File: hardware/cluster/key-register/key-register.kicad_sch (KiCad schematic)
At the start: 2 parts

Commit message: First PCB: the left-hand key board, placed from the body CAD and routed
- tools/pcb.py: a board's first layout from its KiCad sheets (netlist,
  footprints) and the body CAD's new exports (key-board outline DXF,
  switch and ribbon-connector positions); then the .kicad_pcb is source.
  check = KiCad DRC with schematic parity + switches where the CAD puts
  them; render = 3D both sides, 2D copper, and fab/ (Gerbers, drill,
  placement), ledgered in hardware/SHEETS.csv. tools/kicad.py check runs it.
- tools/pcb_route.py: a small two-layer grid router for simple boards;
  ground routed as a net plus pours and stitching vias.
- key-board-lh: 24 parts, all nets routed; KiCad DRC 0 errors, schematic
  parity clean (one stock-footprint silkscreen warning). Tested: a switch
  moved 1 mm fails the check.
- Footprints on the sheets; hardware/lib/woody.pretty holds the KS-33
  footprint (marbastlib, banked) with Gateron's STEP lifted by
  switch.pcb_below_seat. J-CHAIN's stand-in is Molex 200528-0120.
- Findings, recorded in tooling.md §4 and DESIGN.md: the ribbon connector
  needs 6.7 mm, the CAD envelope is 5.5; KS-33 pins show only ~0.1 mm
  below a 1.6 mm board (1.2 mm would leave ~0.5).
- setup-env.sh installs footprints, rsvg, shapely and repairs an empty
  global fp-lib-table.

Co-Authored-By: Claude Opus 5.5 <noreply@anthropic.com>
Claude-Session: https://claude.ai/code/session_01LmB4muFXnoLprWX4JzuJ5A
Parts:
- C-DECOUPLE-165: footprint (none) -> Capacitor_SMD:C_0805_2012Metric
- U-KEYS: footprint (none) -> Package_SO:SOIC-16_3.9x9.9mm_P1.27mm
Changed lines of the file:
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@@
     (property "Reference" "U-KEYS" (at 93.98 91.44 0) (effects (font (size 1.27 1.27))))
     (property "Value" "74HC165" (at 93.98 132.08 0) (effects (font (size 1.27 1.27))))
-    (property "Footprint" "" (at 101.6 110.49 0) (effects (font (size 1.27 1.27)) hide))
+    (property "Footprint" "Package_SO:SOIC-16_3.9x9.9mm_P1.27mm" (at 101.6 110.49 0) (effects (font (size 1.27 1.27)) hide))
     (property "Datasheet" "" (at 101.6 110.49 0) (effects (font (size 1.27 1.27)) hide))
     (property "Row" "U-KEYS" (at 101.6 110.49 0) (effects (font (size 1.27 1.27)) hide))
@@
     (property "Reference" "C-DECOUPLE-165" (at 129.54 78.74 0) (effects (font (size 1.27 1.27)) (justify left)))
     (property "Value" "100nF" (at 129.54 81.28 0) (effects (font (size 1.27 1.27)) (justify left)))
-    (property "Footprint" "" (at 128.27 83.82 0) (effects (font (size 1.27 1.27)) hide))
+    (property "Footprint" "Capacitor_SMD:C_0805_2012Metric" (at 128.27 83.82 0) (effects (font (size 1.27 1.27)) hide))
     (property "Datasheet" "" (at 127.0 80.01 0) (effects (font (size 1.27 1.27)) hide))
     (property "Row" "C-DECOUPLE-165" (at 127.0 80.01 0) (effects (font (size 1.27 1.27)) hide))

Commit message: LH key board as the worked example: orderable, labelled, testable
- Samtec full prints banked (SHF header, FFSD cable); the header's true
  dimensions replace the catalogue estimates (body.yaml boards.chain_*), and
  the cable is ordered -RN2 (notch reversed on the key-board end): both
  sockets' cables leave downward, the ribbon runs flat, and key-board pin =
  13 - main-board pin. The same-day 12-n/14-n map was wrong and is undone in
  the sheets, the interface netlist and the docs (history in notes.md).
- Model: the hairpin's legs follow the cable's real exit - the main board's
  on the board, clear of the thumb switches' poles; 0 DRC FAILs, 0 clashes.
- Sheets: Manufacturer/MPN/LCSC/Assembly fields from JLC's parts API (JLC
  and LCSC pages banked in datasheets/fab and the manifest); five bring-up
  test pads per key board (TP-CHAIN, copper only).
- pcb.py: JLC's limits in the DRC (layout.yaml fab:), which grew the vias
  and J-CHAIN's pads to the 0.18 mm ring; HASL lead-free in the stackup and
  Gerber job; a generated parts-side silkscreen; the JLC BOM, CPL and
  hand-assembly list in fab/, ledgered against board and sheets.
- Router: a real rip-up (blockers removed too); plated holes no longer wall
  off their own pads.
- hardware/boards/key-board-lh/README.md: sources, ordering, hand assembly,
  bring-up, open items. tooling.md and lib README follow.
All checks pass: CAD, DRC (0/0), KiCad, staleness, BOM, netlist, datasheets.

Co-Authored-By: Claude Opus 5.5 <noreply@anthropic.com>
Claude-Session: https://claude.ai/code/session_01LmB4muFXnoLprWX4JzuJ5A
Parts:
- C-DECOUPLE-165: Assembly (none) -> machine; LCSC (none) -> C49678; MPN (none) -> CC0805KRX7R9BB104; Manufacturer (none) -> YAGEO
- U-KEYS: Assembly (none) -> machine; LCSC (none) -> C5613; MPN (none) -> 74HC165D,653; Manufacturer (none) -> Nexperia
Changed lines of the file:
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@@
     (property "Note" "74HC AND NOT 74LVC, and that is load-bearing: HC's slow edges keep each hop an ordinary lumped load. Bit order out is H first, then G F E D C B A" (at 101.6 110.49 0) (effects (font (size 1.27 1.27)) hide))
     (property "Pins_source" "SOIC-16 pin-out, datasheets/logic/74HC165-ti-scls116e.pdf p.1; library names checked" (at 101.6 110.49 0) (effects (font (size 1.27 1.27)) hide))
+    (property "Manufacturer" "Nexperia" (at 101.6 110.49 0) (effects (font (size 1.27 1.27)) hide))
+    (property "MPN" "74HC165D,653" (at 101.6 110.49 0) (effects (font (size 1.27 1.27)) hide))
+    (property "LCSC" "C5613" (at 101.6 110.49 0) (effects (font (size 1.27 1.27)) hide))
+    (property "Assembly" "machine" (at 101.6 110.49 0) (effects (font (size 1.27 1.27)) hide))
     (pin "1")
     (pin "10")
@@
     (property "Pins" "1=1 2=2" (at 127.0 80.01 0) (effects (font (size 1.27 1.27)) hide))
     (property "Note" "AT the package, on this board. A 74x165's output edges brown out a local rail with no reservoir, and on a key board the ribbon is the only other source" (at 127.0 80.01 0) (effects (font (size 1.27 1.27)) hide))
+    (property "Manufacturer" "YAGEO" (at 127.0 80.01 0) (effects (font (size 1.27 1.27)) hide))
+    (property "MPN" "CC0805KRX7R9BB104" (at 127.0 80.01 0) (effects (font (size 1.27 1.27)) hide))
+    (property "LCSC" "C49678" (at 127.0 80.01 0) (effects (font (size 1.27 1.27)) hide))
+    (property "Assembly" "machine" (at 127.0 80.01 0) (effects (font (size 1.27 1.27)) hide))
     (pin "1")
     (pin "2")

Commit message: WIP: layout-side fixes (networks as T, via-in-pad, segment merge, silk, stackup, TP-SER, drills)
Co-Authored-By: Claude Opus 5.5 <noreply@anthropic.com>
Claude-Session: https://claude.ai/code/session_01LmB4muFXnoLprWX4JzuJ5A
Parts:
- U-KEYS: Pins_source SOIC-16 pin-out, datasheets/logic/74HC165-ti-scls116e.pdf p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 -> SO16 (SOT109-1) pin-out, datasheets/logic/74HC165-nexperia.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
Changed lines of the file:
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@@
     (property "Pins" "SHLD=1(~{PL}) CLK=2(CP) CLKINH=15(~{CE}) QH_BAR=7(~{Q7}) GND=8(GND) SER=10(DS) QH=9(Q7) VCC=16(VCC) A=11(D0) B=12(D1) C=13(D2) D=14(D3) E=3(D4) F=4(D5) G=5(D6) H=6(D7)" (at 101.6 110.49 0) (effects (font (size 1.27 1.27)) hide))
     (property "Note" "74HC AND NOT 74LVC, and that is load-bearing: HC's slow edges keep each hop an ordinary lumped load. Bit order out is H first, then G F E D C B A" (at 101.6 110.49 0) (effects (font (size 1.27 1.27)) hide))
-    (property "Pins_source" "SOIC-16 pin-out, datasheets/logic/74HC165-ti-scls116e.pdf p.1; library names checked" (at 101.6 110.49 0) (effects (font (size 1.27 1.27)) hide))
+    (property "Pins_source" "SO16 (SOT109-1) pin-out, datasheets/logic/74HC165-nexperia.pdf p.3 figure and p.4 Table 2; library names checked" (at 101.6 110.49 0) (effects (font (size 1.27 1.27)) hide))
     (property "Manufacturer" "Nexperia" (at 101.6 110.49 0) (effects (font (size 1.27 1.27)) hide))
     (property "MPN" "74HC165D,653" (at 101.6 110.49 0) (effects (font (size 1.27 1.27)) hide))

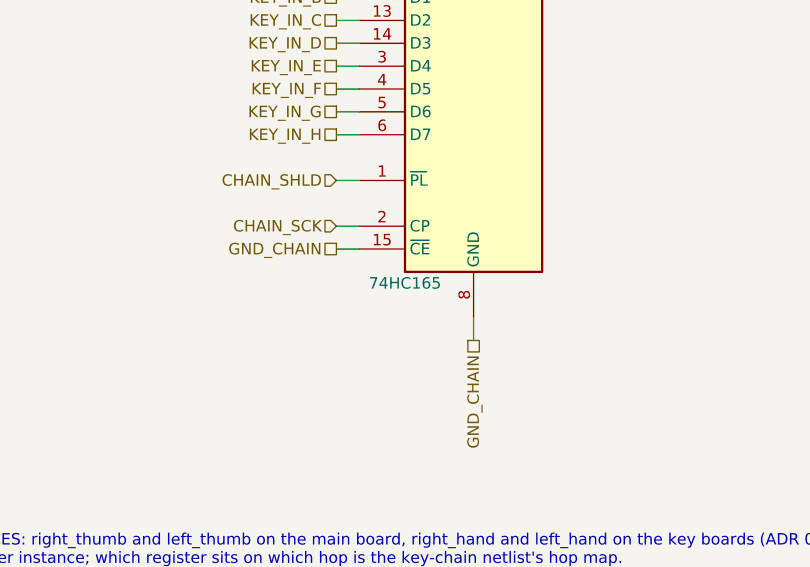
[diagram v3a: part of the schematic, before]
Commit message: Register becomes the SN74HCS165; key-board standoff gets its washer
The owner's two decisions after the LH wave:

SN74HCS165 (TI, Schmitt-trigger inputs, no input transition-rate limit):
- key-register.kicad_sch U-KEYS: value, Manufacturer, MPN SN74HCS165DR,
  LCSC C2864745, Pins_source (TI p.3), Note; same SOIC-16 and symbol.
- U-KEYS row: what the part must be, and that a substitute needs Schmitt
  inputs with no rate limit (not a 74HC165, not a 74LV165A).
- key-release-time 119.9 -> 138.7 us and key-press-time 5.92 -> 9.87 us,
  against TI's thresholds at their guaranteed extremes (no 3.3 V row: the
  table's largest VT+ and smallest VT- ratios). Old spellings grepped first
  and moved into forbidden; the four patterns that matched the new value
  removed. The release is now just over half a scan, which changes no
  conclusion; the 10k trade recomputed (647 us).
- key-switch-network.md derives both against the HCS165; the retired HC165
  derivation moved to notes.md. ADR 0001 amended and its table cites the
  figures.

The standoff and washer:
- MSO4-M2-3 chosen, with an ISO 7092 / DIN 433 M2 washer under the board.
  Head flush in the plate, so the key boards' depth is standoff length +
  washer: switch.pcb_below_seat 3.4 -> 3.3, checked by a new rule, with the
  worst-case tolerance stack printed as a NOTE.
- The thumb switches keep their own depth, switch.thumb_pcb_below_seat:
  sharing the parameter moved them into the LED strip (clash.txt caught it).
- MECH-KB-WASHER row; MECH-KB-STANDOFF names the part and its US sources;
  MECH-KB-SCREW M2 x 4. The PCB's copper keep-out covers the washer.
- LH board re-laid out, checked (0 errors) and rendered.

Co-Authored-By: Claude Opus 5.5 <noreply@anthropic.com>
Claude-Session: https://claude.ai/code/session_01LmB4muFXnoLprWX4JzuJ5A
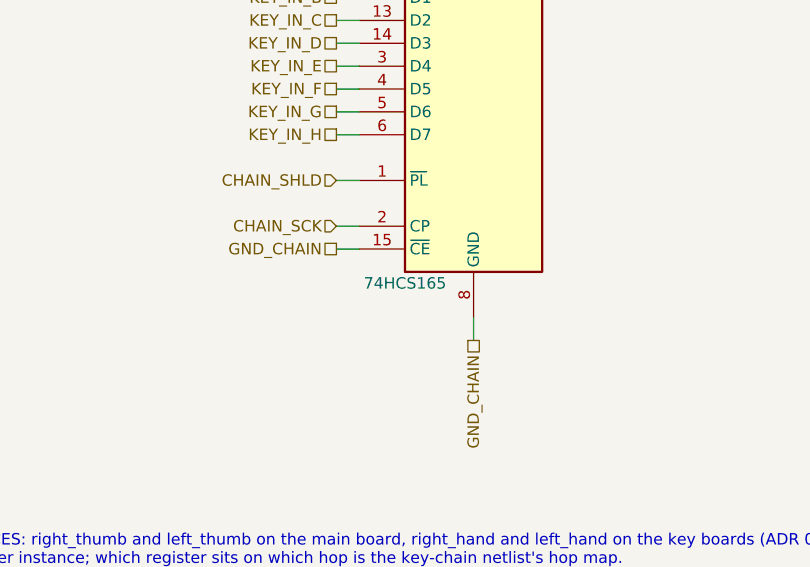
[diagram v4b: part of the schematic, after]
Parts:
- U-KEYS: value 74HC165 -> 74HCS165; LCSC C5613 -> C2864745; MPN 74HC165D,653 -> SN74HCS165DR; Manufacturer Nexperia -> Texas Instruments; Note 74HC AND NOT 74LVC, and that is load-bearing: HC's slow edg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 -> Schmitt-trigger inputs (74HCS): the key networks' slow edge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; Pins_source SO16 (SOT109-1) pin-out, datasheets/logic/74HC165-nexperia.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 -> SOIC-16 (D) pin-out, datasheets/logic/SN74HCS165-ti-scls828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
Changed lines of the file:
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@@
     (in_bom yes) (on_board yes) (dnp no)
     (property "Reference" "U-KEYS" (at 93.98 91.44 0) (effects (font (size 1.27 1.27))))
-    (property "Value" "74HC165" (at 93.98 132.08 0) (effects (font (size 1.27 1.27))))
+    (property "Value" "74HCS165" (at 93.98 132.08 0) (effects (font (size 1.27 1.27))))
     (property "Footprint" "Package_SO:SOIC-16_3.9x9.9mm_P1.27mm" (at 101.6 110.49 0) (effects (font (size 1.27 1.27)) hide))
     (property "Datasheet" "" (at 101.6 110.49 0) (effects (font (size 1.27 1.27)) hide))
     (property "Row" "U-KEYS" (at 101.6 110.49 0) (effects (font (size 1.27 1.27)) hide))
     (property "Pins" "SHLD=1(~{PL}) CLK=2(CP) CLKINH=15(~{CE}) QH_BAR=7(~{Q7}) GND=8(GND) SER=10(DS) QH=9(Q7) VCC=16(VCC) A=11(D0) B=12(D1) C=13(D2) D=14(D3) E=3(D4) F=4(D5) G=5(D6) H=6(D7)" (at 101.6 110.49 0) (effects (font (size 1.27 1.27)) hide))
-    (property "Note" "74HC AND NOT 74LVC, and that is load-bearing: HC's slow edges keep each hop an ordinary lumped load. Bit order out is H first, then G F E D C B A" (at 101.6 110.49 0) (effects (font (size 1.27 1.27)) hide))
-    (property "Pins_source" "SO16 (SOT109-1) pin-out, datasheets/logic/74HC165-nexperia.pdf p.3 figure and p.4 Table 2; library names checked" (at 101.6 110.49 0) (effects (font (size 1.27 1.27)) hide))
-    (property "Manufacturer" "Nexperia" (at 101.6 110.49 0) (effects (font (size 1.27 1.27)) hide))
-    (property "MPN" "74HC165D,653" (at 101.6 110.49 0) (effects (font (size 1.27 1.27)) hide))
-    (property "LCSC" "C5613" (at 101.6 110.49 0) (effects (font (size 1.27 1.27)) hide))
+    (property "Note" "Schmitt-trigger inputs (74HCS): the key networks' slow edges are within its rating - it has no input transition-rate limit. HC-family outputs, not LVC: its edges keep each hop an ordinary lumped load. Bit order out is H first, then G F E D C B A" (at 101.6 110.49 0) (effects (font (size 1.27 1.27)) hide))
+    (property "Pins_source" "SOIC-16 (D) pin-out, datasheets/logic/SN74HCS165-ti-scls828a.pdf p.3 section 5; identical to the 74HC165's; library symbol 74xx:74HC165 names checked" (at 101.6 110.49 0) (effects (font (size 1.27 1.27)) hide))
+    (property "Manufacturer" "Texas Instruments" (at 101.6 110.49 0) (effects (font (size 1.27 1.27)) hide))
+    (property "MPN" "SN74HCS165DR" (at 101.6 110.49 0) (effects (font (size 1.27 1.27)) hide))
+    (property "LCSC" "C2864745" (at 101.6 110.49 0) (effects (font (size 1.27 1.27)) hide))
     (property "Assembly" "machine" (at 101.6 110.49 0) (effects (font (size 1.27 1.27)) hide))
     (pin "1")

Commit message: Wave r2 fixes, part 1: board tools, the T's orientation, the decoupling loop; docs
Tools (docs/review/2026-09-27-lh-key-board-r2, closed by id in its STATUS.md):
- network_parts: the axis-y rotation was the wrong way round (R6-3), so
  every S and P faced its KEY pad away from the junction; fixed, with a
  layout-time assert that each T's three nearest pads are its node, and
  validation of networks: (R6-9).
- check_tracks sees a branch ending mid-track, and exempts a wedge whose
  apex a via or pad fills (R6-1, R6-7, R3-4); square_joins splits such a
  track first, keeps the router's copper list current, tests holes,
  keep-outs and the edge, and warns at its pass limit (R6-6).
- Vias keep off silkscreen (the router takes the silk as via obstacles),
  and check_silk fails silk on a via and filled slivers (R3-2, R3-3, R6-8,
  R6-13).
- Any DRC test set to ignore fails unless allowlisted with its reason
  (R6-2); check proves the standoff keep-outs hold no copper and the holes
  are NPTH at the CAD's size (R6-4).
- connect_first: the decoupler's return routed first to the register's
  ground pin 8 (not pin 15, CLK INH), held to 15 mm by check (R3-1) - now
  10.4 mm of track.
- Stitching vias skipped only on the main ground tree (R6-5); one stub per
  pad (R3-7); silk stroke 0.18 (R3-8); removed library silk is reported
  (R6-12). Test pads QH/SER in pin order (R3-9).

Docs (R1, R5 non-mechanical): the glitch-filter, lumped-load, R-KEY-SER
ceiling and scan-latency arguments restated against the right limits;
forbidden patterns for the retired thresholds in their CSV spellings.

Co-Authored-By: Claude Opus 5.5 <noreply@anthropic.com>
Claude-Session: https://claude.ai/code/session_01LmB4muFXnoLprWX4JzuJ5A
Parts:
- U-KEYS: Note Schmitt-trigger inputs (74HCS): the key networks' slow edges are within its rating - it has no input transition-rate limit. HC-family outputs, not LVC: its edges keep each hop an ordinary lumped load. Bit order out is H first, then G F E D C B A -> Schmitt-trigger inputs (74HCS): the key networks' slow edges are within its rating - it has no input transition-rate limit. HC-family outputs, not LVC: the weaker drive. A hop is not a lumped load and need not be - QH to the next SER is data sampled a clock period later, into a Schmitt input (key-register.md). Bit order out is H first, then G F E D C B A
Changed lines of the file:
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@@
     (property "Row" "U-KEYS" (at 101.6 110.49 0) (effects (font (size 1.27 1.27)) hide))
     (property "Pins" "SHLD=1(~{PL}) CLK=2(CP) CLKINH=15(~{CE}) QH_BAR=7(~{Q7}) GND=8(GND) SER=10(DS) QH=9(Q7) VCC=16(VCC) A=11(D0) B=12(D1) C=13(D2) D=14(D3) E=3(D4) F=4(D5) G=5(D6) H=6(D7)" (at 101.6 110.49 0) (effects (font (size 1.27 1.27)) hide))
-    (property "Note" "Schmitt-trigger inputs (74HCS): the key networks' slow edges are within its rating - it has no input transition-rate limit. HC-family outputs, not LVC: its edges keep each hop an ordinary lumped load. Bit order out is H first, then G F E D C B A" (at 101.6 110.49 0) (effects (font (size 1.27 1.27)) hide))
+    (property "Note" "Schmitt-trigger inputs (74HCS): the key networks' slow edges are within its rating - it has no input transition-rate limit. HC-family outputs, not LVC: the weaker drive. A hop is not a lumped load and need not be - QH to the next SER is data sampled a clock period later, into a Schmitt input (key-register.md). Bit order out is H first, then G F E D C B A" (at 101.6 110.49 0) (effects (font (size 1.27 1.27)) hide))
     (property "Pins_source" "SOIC-16 (D) pin-out, datasheets/logic/SN74HCS165-ti-scls828a.pdf p.3 section 5; identical to the 74HC165's; library symbol 74xx:74HC165 names checked" (at 101.6 110.49 0) (effects (font (size 1.27 1.27)) hide))
     (property "Manufacturer" "Texas Instruments" (at 101.6 110.49 0) (effects (font (size 1.27 1.27)) hide))
